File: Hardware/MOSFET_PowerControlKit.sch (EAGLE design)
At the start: 11 parts, among them Q1 IRF

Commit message: Added measurements and version #
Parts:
- removed JP7: LOGO-SFESK, SparkFun:LOGO-SFESK
- added LOGO2: SFE_LOGO_FLAME.1_INCH, SparkFun-Aesthetics:SFE_LOGO_FLAME.1_INCH
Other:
- note added: "V11"
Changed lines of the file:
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@@
 <?xml version="1.0" encoding="utf-8"?>
 <!DOCTYPE eagle SYSTEM "eagle.dtd">
-<eagle version="6.5.0">
+<eagle version="6.4">
 <drawing>
 <settings>
@@
 <grid distance="0.1" unitdist="inch" unit="inch" style="lines" multiple="1" display="no" altdistance="0.01" altunitdist="inch" altunit="inch"/>
 <layers>
-<layer number="1" name="Top" color="4" fill="1" visible="yes" active="no"/>
-<layer number="2" name="Route2" color="1" fill="3" visible="yes" active="no"/>
-<layer number="3" name="Route3" color="4" fill="3" visible="yes" active="no"/>
-<layer number="4" name="Route4" color="1" fill="4" visible="yes" active="no"/>
-<layer number="5" name="Route5" color="4" fill="4" visible="yes" active="no"/>
-<layer number="6" name="Route6" color="1" fill="8" visible="yes" active="no"/>
-<layer number="7" name="Route7" color="4" fill="8" visible="yes" active="no"/>
-<layer number="8" name="Route8" color="1" fill="2" visible="yes" active="no"/>
-<layer number="9" name="Route9" color="4" fill="2" visible="yes" active="no"/>
-<layer number="10" name="Route10" color="1" fill="7" visible="yes" active="no"/>
-<layer number="11" name="Route11" color="4" fill="7" visible="yes" active="no"/>
-<layer number="12" name="Route12" color="1" fill="5" visible="yes" active="no"/>
-<layer number="13" name="Route13" color="4" fill="5" visible="yes" active="no"/>
-<layer number="14" name="Route14" color="1" fill="6" visible="yes" active="no"/>
-<layer number="15" name="Route15" color="4" fill="6" visible="yes" active="no"/>
-<layer number="16" name="Bottom" color="1" fill="1" visible="yes" active="no"/>
-<layer number="17" name="Pads" color="2" fill="1" visible="yes" active="no"/>
-<layer number="18" name="Vias" color="2" fill="1" visible="yes" active="no"/>
-<layer number="19" name="Unrouted" color="6" fill="1" visible="yes" active="no"/>
-<layer number="20" name="Dimension" color="15" fill="1" visible="yes" active="no"/>
-<layer number="21" name="tPlace" color="16" fill="1" visible="yes" active="no"/>
-<layer number="22" name="bPlace" color="14" fill="1" visible="yes" active="no"/>
-<layer number="23" name="tOrigins" color="15" fill="1" visible="yes" active="no"/>
-<layer number="24" name="bOrigins" color="15" fill="1" visible="yes" active="no"/>
-<layer number="25" name="tNames" color="7" fill="1" visible="yes" active="no"/>
-<layer number="26" name="bNames" color="7" fill="1" visible="yes" active="no"/>
-<layer number="27" name="tValues" color="7" fill="1" visible="yes" active="no"/>
-<layer number="28" name="bValues" color="7" fill="1" visible="yes" active="no"/>
+<layer number="1" name="Top" color="4" fill="1" visible="no" active="no"/>
+<layer number="2" name="Route2" color="1" fill="3" visible="no" active="no"/>
+<layer number="3" name="Route3" color="4" fill="3" visible="no" active="no"/>
+<layer number="4" name="Route4" color="1" fill="4" visible="no" active="no"/>
+<layer number="5" name="Route5" color="4" fill="4" visible="no" active="no"/>
+<layer number="6" name="Route6" color="1" fill="8" visible="no" active="no"/>
+<layer number="7" name="Route7" color="4" fill="8" visible="no" active="no"/>
+<layer number="8" name="Route8" color="1" fill="2" visible="no" active="no"/>
+<layer number="9" name="Route9" color="4" fill="2" visible="no" active="no"/>
+<layer number="10" name="Route10" color="1" fill="7" visible="no" active="no"/>
+<layer number="11" name="Route11" color="4" fill="7" visible="no" active="no"/>
+<layer number="12" name="Route12" color="1" fill="5" visible="no" active="no"/>
+<layer number="13" name="Route13" color="4" fill="5" visible="no" active="no"/>
+<layer number="14" name="Route14" color="1" fill="6" visible="no" active="no"/>
+<layer number="15" name="Route15" color="4" fill="6" visible="no" active="no"/>
+<layer number="16" name="Bottom" color="1" fill="1" visible="no" active="no"/>
+<layer number="17" name="Pads" color="2" fill="1" visible="no" active="no"/>
+<layer number="18" name="Vias" color="2" fill="1" visible="no" active="no"/>
+<layer number="19" name="Unrouted" color="6" fill="1" visible="no" active="no"/>
+<layer number="20" name="Dimension" color="15" fill="1" visible="no" active="no"/>
+<layer number="21" name="tPlace" color="16" fill="1" visible="no" active="no"/>
+<layer number="22" name="bPlace" color="14" fill="1" visible="no" active="no"/>
+<layer number="23" name="tOrigins" color="15" fill="1" visible="no" active="no"/>
+<layer number="24" name="bOrigins" color="15" fill="1" visible="no" active="no"/>
+<layer number="25" name="tNames" color="7" fill="1" visible="no" active="no"/>
+<layer number="26" name="bNames" color="7" fill="1" visible="no" active="no"/>
+<layer number="27" name="tValues" color="7" fill="1" visible="no" active="no"/>
+<layer number="28" name="bValues" color="7" fill="1" visible="no" active="no"/>
 <layer number="29" name="tStop" color="7" fill="3" visible="no" active="no"/>
 <layer number="30" name="bStop" color="7" fill="6" visible="no" active="no"/>
@@
 <layer number="35" name="tGlue" color="7" fill="4" visible="no" active="no"/>
 <layer number="36" name="bGlue" color="7" fill="5" visible="no" active="no"/>
-<layer number="37" name="tTest" color="7" fill="1" visible="yes" active="no"/>
-<layer number="38" name="bTest" color="7" fill="1" visible="yes" active="no"/>
+<layer number="37" name="tTest" color="7" fill="1" visible="no" active="no"/>
+<layer number="38" name="bTest" color="7" fill="1" visible="no" active="no"/>
 <layer number="39" name="tKeepout" color="4" fill="11" visible="no" active="no"/>
 <layer number="40" name="bKeepout" color="1" fill="11" visible="no" active="no"/>
@@
 <layer number="44" name="Drills" color="7" fill="1" visible="no" active="no"/>
 <layer number="45" name="Holes" color="7" fill="1" visible="no" active="no"/>
-<layer number="46" name="Milling" color="3" fill="1" visible="yes" active="no"/>
-<layer number="47" name="Measures" color="7" fill="1" visible="yes" active="no"/>
-<layer number="48" name="Document" color="7" fill="1" visible="yes" active="no"/>
-<layer number="49" name="Reference" color="7" fill="1" visible="yes" active="no"/>
-<layer number="50" name="dxf" color="7" fill="1" visible="yes" active="no"/>
-<layer number="51" name="tDocu" color="6" fill="1" visible="yes" active="no"/>
-<layer number="52" name="bDocu" color="7" fill="1" visible="yes" active="no"/>
-<layer number="53" name="tGND_GNDA" color="7" fill="9" visible="yes" active="no"/>
-<layer number="54" name="bGND_GNDA" color="1" fill="9" visible="yes" active="no"/>
-<layer number="56" name="wert" color="7" fill="1" visible="yes" active="no"/>
-<layer number="57" name="tCAD" color="7" fill="1" visible="yes" active="no"/>
+<layer number="46" name="Milling" color="3" fill="1" visible="no" active="no"/>
+<layer number="47" name="Measures" color="7" fill="1" visible="no" active="no"/>
+<layer number="48" name="Document" color="7" fill="1" visible="no" active="no"/>
+<layer number="49" name="Reference" color="7" fill="1" visible="no" active="no"/>
+<layer number="50" name="dxf" color="7" fill="1" visible="no" active="no"/>
+<layer number="51" name="tDocu" color="6" fill="1" visible="no" active="no"/>
+<layer number="52" name="bDocu" color="7" fill="1" visible="no" active="no"/>
+<layer number="53" name="tGND_GNDA" color="7" fill="9" visible="no" active="no"/>
+<layer number="54" name="bGND_GNDA" color="1" fill="9" visible="no" active="no"/>
+<layer number="56" name="wert" color="7" fill="1" visible="no" active="no"/>
+<layer number="57" name="tCAD" color="7" fill="1" visible="no" active="no"/>
 <layer number="91" name="Nets" color="2" fill="1" visible="yes" active="yes"/>
 <layer number="92" name="Busses" color="1" fill="1" visible="yes" active="yes"/>
@@
 <part name="GND1" library="SparkFun" deviceset="GND" device=""/>
 <part name="GND5" library="SparkFun" deviceset="GND" device=""/>
-<part name="JP7" library="SparkFun" deviceset="LOGO-SFE" device="SK"/>
 <part name="JP8" library="SparkFun" deviceset="M02" device="JST-PTH-2"/>
 <part name="P+1" library="SparkFun" deviceset="VCC" device="" value="RAW"/>
@@
 <part name="JP5" library="SparkFun" deviceset="M03" device="PTH"/>
 <part name="LOGO1" library="SparkFun-Aesthetics" deviceset="OSHW-LOGO" device="S"/>
+<part name="LOGO2" library="SparkFun-Aesthetics" deviceset="SFE_LOGO_FLAME" device=".1_INCH"/>
 </parts>
 <sheets>
@@
 <text x="170.942" y="11.176" size="2.54" layer="94">N. Seidle</text>
 <text x="148.844" y="6.858" size="2.54" layer="94">Revised by: Patrick Alberts</text>
+<text x="238.76" y="7.62" size="1.778" layer="94">V11</text>
 </plain>
 <instances>
@@
 <instance part="GND1" gate="1" x="93.98" y="83.82"/>
 <instance part="GND5" gate="1" x="104.14" y="83.82"/>
-<instance part="JP7" gate="G$1" x="241.3" y="25.4"/>
 <instance part="JP8" gate="G$1" x="114.3" y="119.38" rot="MR0"/>
 <instance part="P+1" gate="1" x="76.2" y="109.22"/>
@@
 <instance part="JP5" gate="G$1" x="88.9" y="63.5" rot="MR180"/>
 <instance part="LOGO1" gate="G$1" x="236.22" y="45.72"/>
+<instance part="LOGO2" gate="G$1" x="215.9" y="38.1"/>
 </instances>
 <busses>

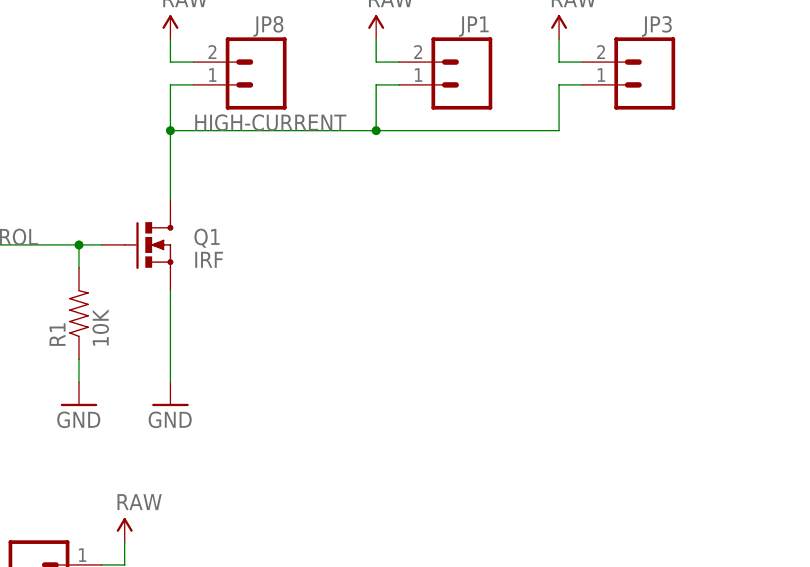
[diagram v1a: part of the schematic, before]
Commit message: Qc checklist fixes
Added max current / voltage to sch
fixed airwire
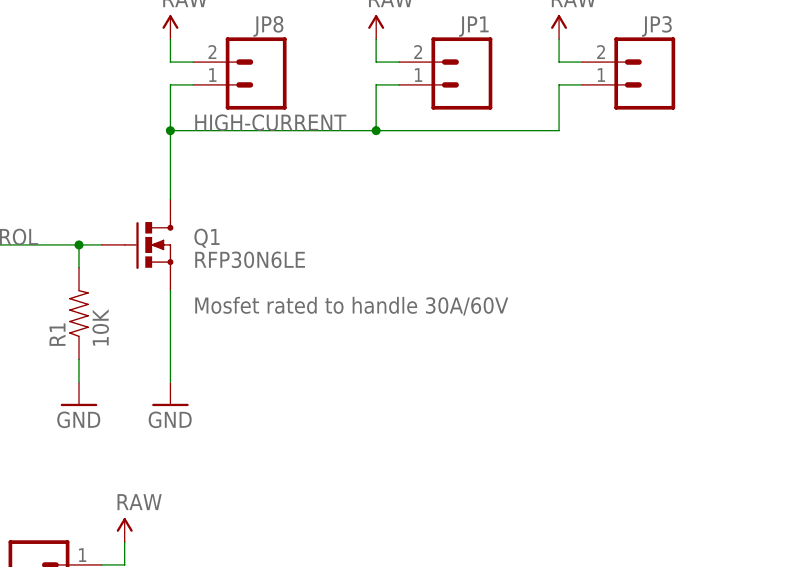
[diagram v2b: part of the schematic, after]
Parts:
- Q1: value IRF -> RFP30N6LE
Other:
- note added: "Mosfet rated to handle 30A/60V"
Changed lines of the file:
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@@
 <parts>
 <part name="FRAME1" library="SparkFun-Aesthetics" deviceset="FRAME-LETTER" device=""/>
-<part name="Q1" library="SparkFun" deviceset="MOSFET-NCHANNEL" device="PTH2" value="IRF"/>
+<part name="Q1" library="SparkFun" deviceset="MOSFET-NCHANNEL" device="PTH2" value="RFP30N6LE"/>
 <part name="R1" library="SparkFun" deviceset="RESISTOR" device="PTH1" value="10K"/>
 <part name="GND1" library="SparkFun" deviceset="GND" device=""/>
@@
 <text x="148.844" y="6.858" size="2.54" layer="94">Revised by: Patrick Alberts</text>
 <text x="238.76" y="7.62" size="1.778" layer="94">V11</text>
+<text x="106.68" y="93.98" size="1.778" layer="95">Mosfet rated to handle 30A/60V</text>
 </plain>
 <instances>

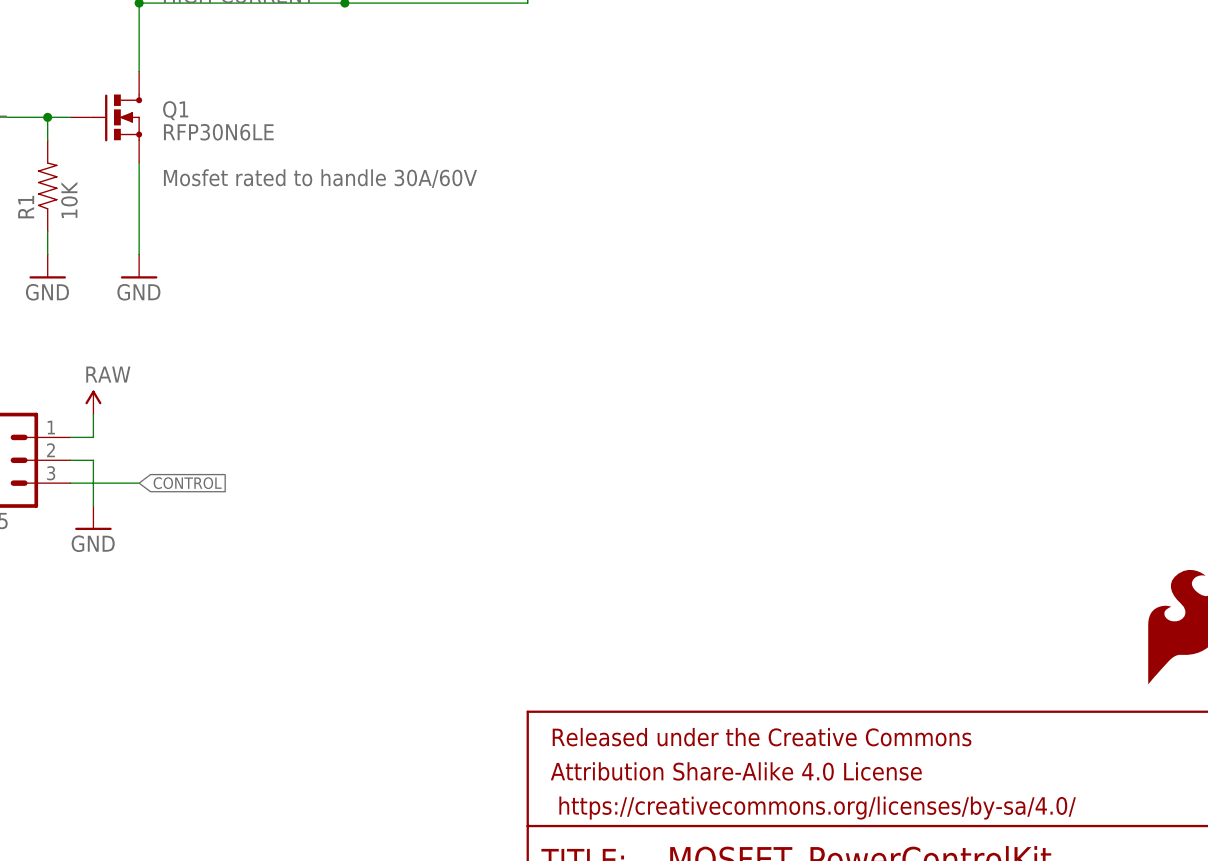
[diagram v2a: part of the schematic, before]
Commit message: More qc checklist changes
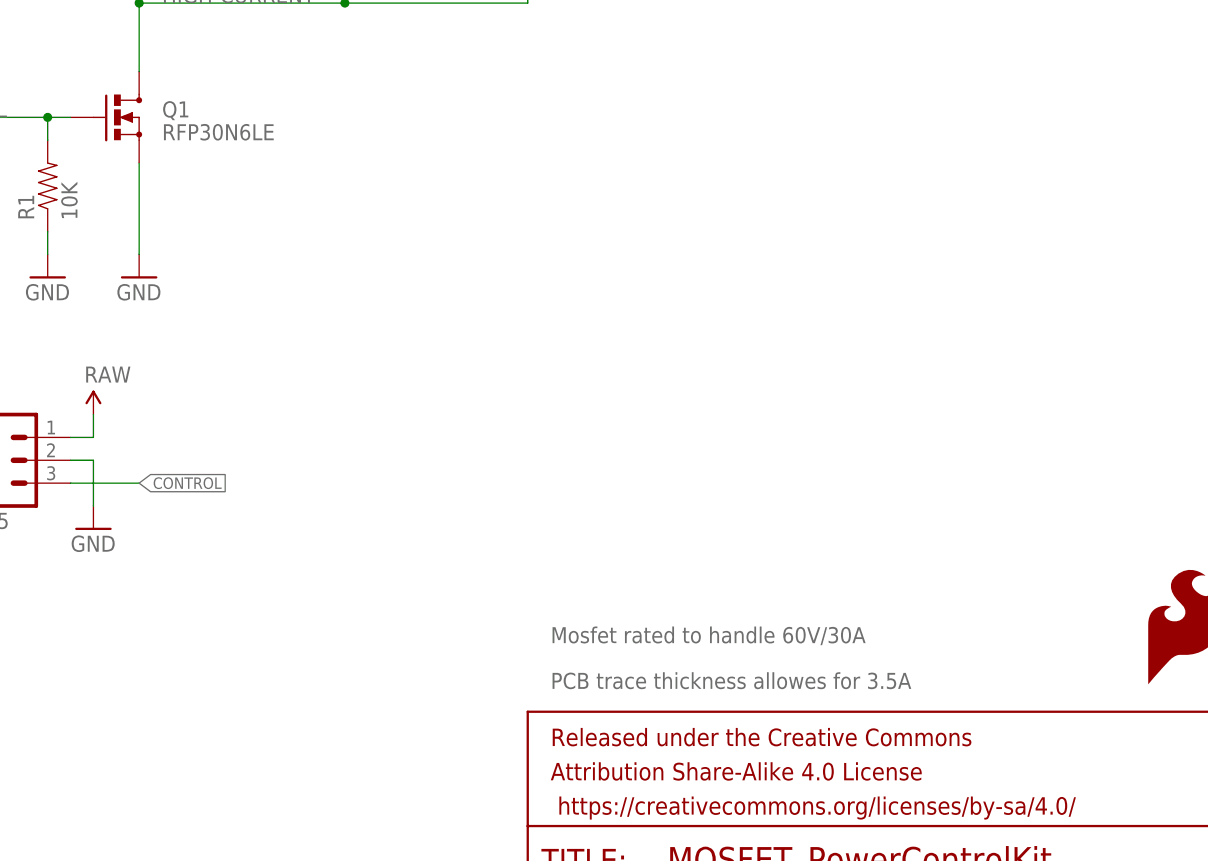
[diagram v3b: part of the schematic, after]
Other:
- note added: "Mosfet rated to handle 60V/30A"
- note added: "PCB trace thickness allowes for 3.5A"
- note removed: "Mosfet rated to handle 30A/60V"
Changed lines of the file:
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@@
 <text x="148.844" y="6.858" size="2.54" layer="94">Revised by: Patrick Alberts</text>
 <text x="238.76" y="7.62" size="1.778" layer="94">V11</text>
-<text x="106.68" y="93.98" size="1.778" layer="95">Mosfet rated to handle 30A/60V</text>
+<text x="149.86" y="43.18" size="1.778" layer="95">Mosfet rated to handle 60V/30A</text>
+<text x="149.86" y="38.1" size="1.778" layer="95">PCB trace thickness allowes for 3.5A</text>
 </plain>
 <instances>
